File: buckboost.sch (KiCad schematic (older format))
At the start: 24 parts, among them K1 CONN_3, SW1 SPST, U1 TPS63060

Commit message: Added preview for XFL4020 Coilcraft footprint.
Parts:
- C1, C2, C3, C4, C5, C6, C7: footprint (none) -> Capacitors_SMD:C_0805_HandSoldering
- D2, D3: footprint (none) -> LEDs:LED_0805
- K1: footprint (none) -> Pin_Headers:Pin_Header_Straight_1x03
- L1: footprint (none) -> XFL4020:XFL4020
- R1, R2, R3, R4, R5, R6, R7, R8: footprint (none) -> Resistors_SMD:R_0805_HandSoldering
- SW1: footprint (none) -> Buttons_Switches_ThroughHole:SW_DIP_x1_Slide
- U1: footprint (none) -> Housings_DFN_QFN:DFN-10-1EP_3x3mm_Pitch0.5mm
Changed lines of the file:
@@
 LIBS:valves
 LIBS:tps63060
+LIBS:buckboost-cache
 EELAYER 25 0
 EELAYER END
@@
 F 0 "U1" H 4950 5000 60  0000 C CNN
 F 1 "TPS63060" H 4950 4200 60  0000 C CNN
-F 2 "" H 4950 4150 60  0000 C CNN
+F 2 "Housings_DFN_QFN:DFN-10-1EP_3x3mm_Pitch0.5mm" H 4950 4150 60  0001 C CNN
 F 3 "" H 4950 4150 60  0000 C CNN
 	1    4950 4150
@@
 F 0 "C2" H 3550 3800 40  0000 L CNN
 F 1 "0.1 uF" H 3556 3615 40  0000 L CNN
-F 2 "" H 3588 3550 30  0000 C CNN
+F 2 "Capacitors_SMD:C_0805_HandSoldering" H 3588 3550 30  0001 C CNN
 F 3 "" H 3550 3700 60  0000 C CNN
 	1    3550 3700
@@
 F 0 "L1" V 4900 3100 40  0000 C CNN
 F 1 "1 uH" V 5050 3100 40  0000 C CNN
-F 2 "" H 4950 3100 60  0000 C CNN
+F 2 "XFL4020:XFL4020" H 4950 3100 60  0001 C CNN
 F 3 "" H 4950 3100 60  0000 C CNN
 	1    4950 3100
@@
 F 0 "C3" H 4150 4400 40  0000 L CNN
 F 1 "0.1 uF" H 4156 4215 40  0000 L CNN
-F 2 "" H 4188 4150 30  0000 C CNN
+F 2 "Capacitors_SMD:C_0805_HandSoldering" H 4188 4150 30  0001 C CNN
 F 3 "" H 4150 4300 60  0000 C CNN
 	1    4150 4300
@@
 F 0 "R4" V 5930 3600 40  0000 C CNN
 F 1 "1M R" V 5857 3601 40  0000 C CNN
-F 2 "" V 5780 3600 30  0000 C CNN
+F 2 "Resistors_SMD:R_0805_HandSoldering" V 5780 3600 30  0001 C CNN
 F 3 "" H 5850 3600 30  0000 C CNN
 	1    5850 3600
@@
 F 0 "C4" H 6350 4050 40  0000 L CNN
 F 1 "10 pF" H 6356 3865 40  0000 L CNN
-F 2 "" H 6388 3800 30  0000 C CNN
+F 2 "Capacitors_SMD:C_0805_HandSoldering" H 6388 3800 30  0001 C CNN
 F 3 "" H 6350 3950 60  0000 C CNN
 	1    6350 3950
@@
 F 0 "R6" V 7030 3950 40  0000 C CNN
 F 1 "1M R" V 6957 3951 40  0000 C CNN
-F 2 "" V 6880 3950 30  0000 C CNN
+F 2 "Resistors_SMD:R_0805_HandSoldering" V 6880 3950 30  0001 C CNN
 F 3 "" H 6950 3950 30  0000 C CNN
 	1    6950 3950
@@
 F 0 "C5" H 8050 3800 40  0000 L CNN
 F 1 "22uF" H 8056 3615 40  0000 L CNN
-F 2 "" H 8088 3550 30  0000 C CNN
+F 2 "Capacitors_SMD:C_0805_HandSoldering" H 8088 3550 30  0001 C CNN
 F 3 "" H 8050 3700 60  0000 C CNN
 	1    8050 3700
@@
 F 0 "C1" H 3200 3800 40  0000 L CNN
 F 1 "10 uF" H 3206 3615 40  0000 L CNN
-F 2 "" H 3238 3550 30  0000 C CNN
+F 2 "Capacitors_SMD:C_0805_HandSoldering" H 3238 3550 30  0001 C CNN
 F 3 "" H 3200 3700 60  0000 C CNN
 	1    3200 3700
@@
 F 0 "C6" H 8300 3800 40  0000 L CNN
 F 1 "22uF" H 8306 3615 40  0000 L CNN
-F 2 "" H 8338 3550 30  0000 C CNN
+F 2 "Capacitors_SMD:C_0805_HandSoldering" H 8338 3550 30  0001 C CNN
 F 3 "" H 8300 3700 60  0000 C CNN
 	1    8300 3700
@@
 F 0 "C7" H 8550 3800 40  0000 L CNN
 F 1 "22uF" H 8556 3615 40  0000 L CNN
-F 2 "" H 8588 3550 30  0000 C CNN
+F 2 "Capacitors_SMD:C_0805_HandSoldering" H 8588 3550 30  0001 C CNN
 F 3 "" H 8550 3700 60  0000 C CNN
 	1    8550 3700
@@
 F 0 "SW1" H 1200 3600 70  0000 C CNN
 F 1 "SPST" H 1200 3400 70  0000 C CNN
-F 2 "" H 1200 3500 60  0000 C CNN
+F 2 "Buttons_Switches_ThroughHole:SW_DIP_x1_Slide" H 1200 3500 60  0001 C CNN
 F 3 "" H 1200 3500 60  0000 C CNN
 	1    1200 3500
@@
 F 0 "D1" H 700 3100 40  0000 C CNN
 F 1 "DIODESCH" H 700 2900 40  0000 C CNN
-F 2 "" H 700 3000 60  0000 C CNN
+F 2 "" H 700 3000 60  0001 C CNN
 F 3 "" H 700 3000 60  0000 C CNN
 	1    700  3000
@@
 F 0 "R5" V 6530 3100 40  0000 C CNN
 F 1 "22k R" V 6457 3101 40  0000 C CNN
-F 2 "" V 6380 3100 30  0000 C CNN
+F 2 "Resistors_SMD:R_0805_HandSoldering" V 6380 3100 30  0001 C CNN
 F 3 "" H 6450 3100 30  0000 C CNN
 	1    6450 3100
@@
 F 0 "D3" H 6850 2950 50  0000 C CNN
 F 1 "LED" H 6850 2750 50  0000 C CNN
-F 2 "" H 6850 2850 60  0000 C CNN
+F 2 "LEDs:LED_0805" H 6850 2850 60  0001 C CNN
 F 3 "" H 6850 2850 60  0000 C CNN
 	1    6850 2850
@@
 F 0 "R3" V 3030 3750 40  0000 C CNN
 F 1 "22k R" V 2957 3751 40  0000 C CNN
-F 2 "" V 2880 3750 30  0000 C CNN
+F 2 "Resistors_SMD:R_0805_HandSoldering" V 2880 3750 30  0001 C CNN
 F 3 "" H 2950 3750 30  0000 C CNN
 	1    2950 3750
@@
 F 0 "D2" H 2950 4400 50  0000 C CNN
 F 1 "LED" H 2950 4200 50  0000 C CNN
-F 2 "" H 2950 4300 60  0000 C CNN
+F 2 "LEDs:LED_0805" H 2950 4300 60  0001 C CNN
 F 3 "" H 2950 4300 60  0000 C CNN
 	1    2950 4300
@@
 F 0 "K1" V 1800 1000 50  0000 C CNN
 F 1 "CONN_3" V 1900 1000 40  0000 C CNN
-F 2 "" H 1850 1000 60  0000 C CNN
+F 2 "Pin_Headers:Pin_Header_Straight_1x03" H 1850 1000 60  0001 C CNN
 F 3 "" H 1850 1000 60  0000 C CNN
 	1    1850 1000
@@
 F 0 "R2" V 1580 1450 40  0000 C CNN
 F 1 "111k R" V 1507 1451 40  0000 C CNN
-F 2 "" V 1430 1450 30  0000 C CNN
+F 2 "Resistors_SMD:R_0805_HandSoldering" V 1430 1450 30  0001 C CNN
 F 3 "" H 1500 1450 30  0000 C CNN
 	1    1500 1450
@@
 F 0 "R1" V 830 1450 40  0000 C CNN
 F 1 "179k R" V 757 1451 40  0000 C CNN
-F 2 "" V 680 1450 30  0000 C CNN
+F 2 "Resistors_SMD:R_0805_HandSoldering" V 680 1450 30  0001 C CNN
 F 3 "" H 750 1450 30  0000 C CNN
 	1    750  1450
@@
 F 0 "FB1" H 2150 3600 50  0000 C CNN
 F 1 "1K @ 100 MHz" H 2150 3450 50  0000 C CNN
-F 2 "" H 2150 3500 60  0000 C CNN
+F 2 "" H 2150 3500 60  0001 C CNN
 F 3 "" H 2150 3500 60  0000 C CNN
 	1    2150 3500
@@
 F 0 "FB2" H 7600 3600 50  0000 C CNN
 F 1 "1K @ 100 MHz" H 7600 3450 50  0000 C CNN
-F 2 "" H 7600 3500 60  0000 C CNN
+F 2 "" H 7600 3500 60  0001 C CNN
 F 3 "" H 7600 3500 60  0000 C CNN
 	1    7600 3500
@@
 F 0 "R8" V 8980 3500 40  0000 C CNN
 F 1 "0.01" V 8907 3501 40  0000 C CNN
-F 2 "" V 8830 3500 30  0000 C CNN
+F 2 "Resistors_SMD:R_0805_HandSoldering" V 8830 3500 30  0001 C CNN
 F 3 "" H 8900 3500 30  0000 C CNN
 	1    8900 3500
@@
 F 0 "R7" V 4180 3500 40  0000 C CNN
 F 1 "0.01" V 4107 3501 40  0000 C CNN
-F 2 "" V 4030 3500 30  0000 C CNN
+F 2 "Resistors_SMD:R_0805_HandSoldering" V 4030 3500 30  0001 C CNN
 F 3 "" H 4100 3500 30  0000 C CNN
 	1    4100 3500

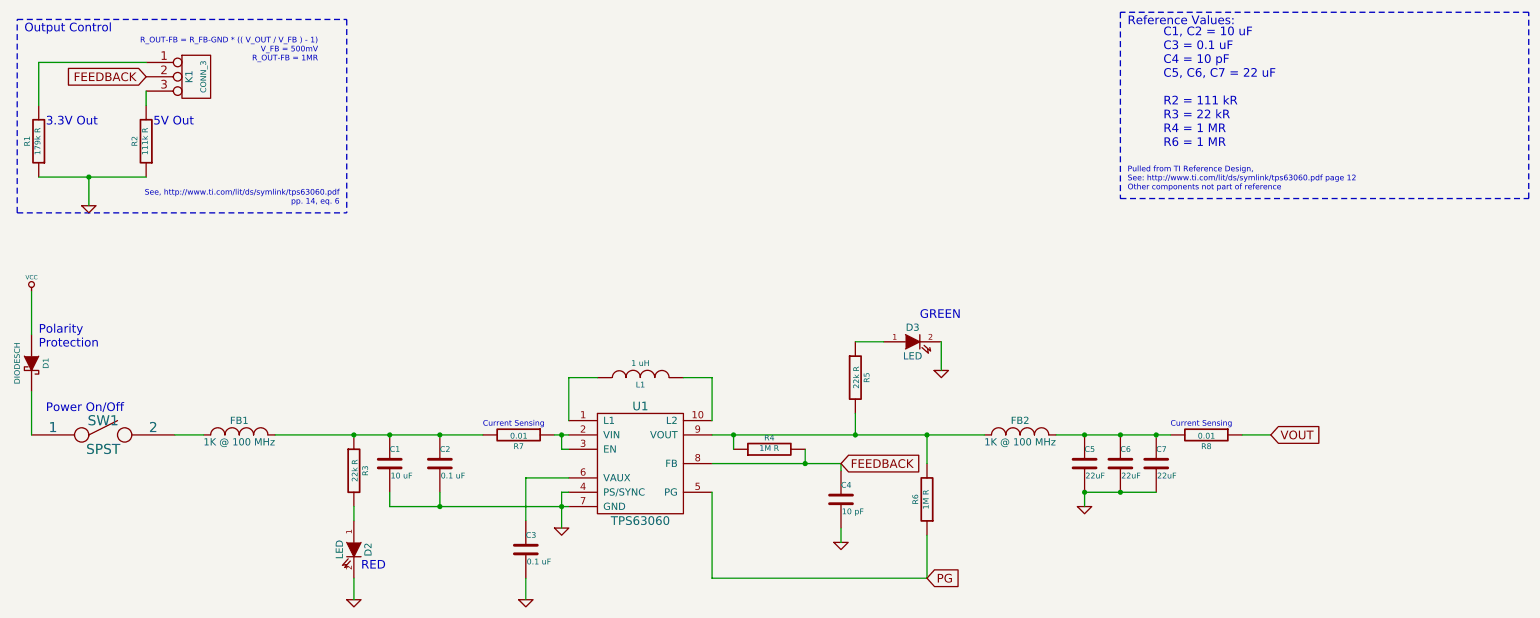
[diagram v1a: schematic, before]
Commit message: Footprints chosen, PCB starting. No preview.
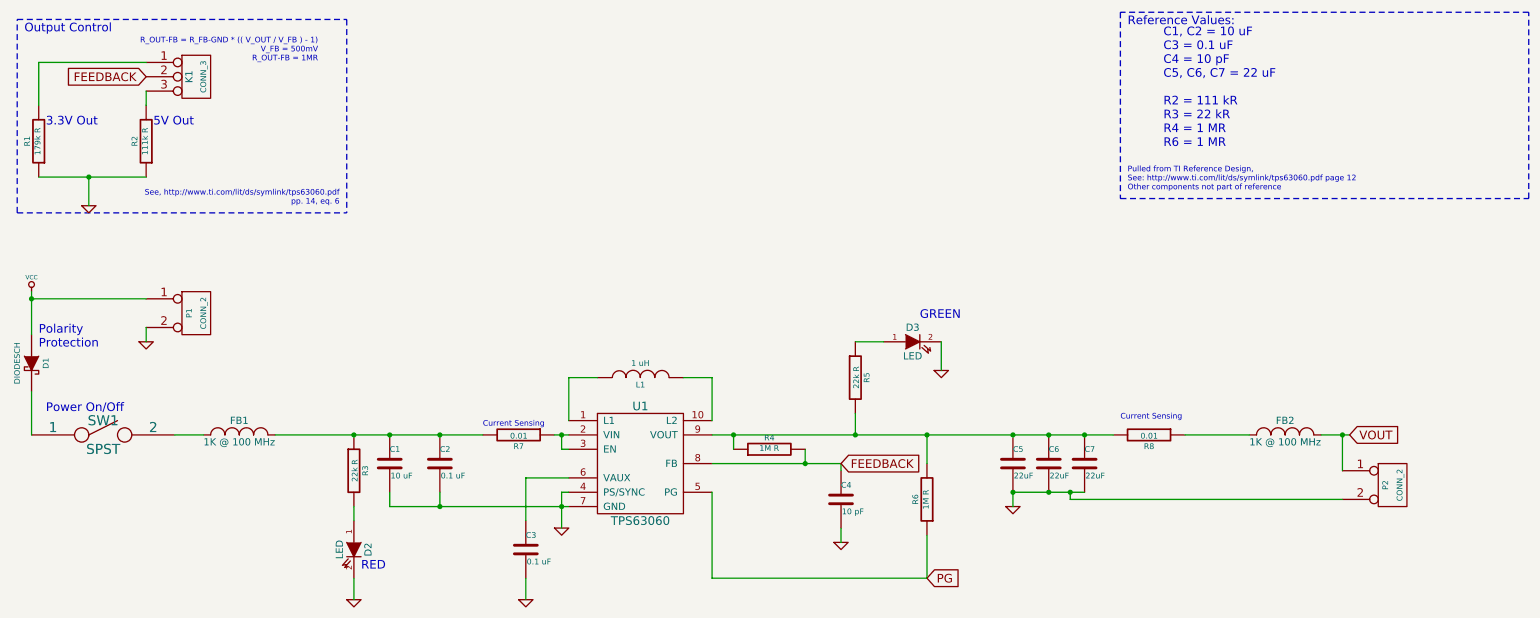
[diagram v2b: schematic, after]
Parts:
- added P1, P2: CONN_2, Pin_Headers:Pin_Header_Straight_1x02, symbol CONN_2
- D1: footprint (none) -> Capacitors_SMD:C_1206_HandSoldering
- FB1, FB2: footprint (none) -> Capacitors_SMD:C_1210_HandSoldering
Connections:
- net GND: now also P1.2 (PM), P2.2 (PM)
- net VCC: now also P1.1 (P1)
- net VOUT: now also FB2.2, P2.1 (P1); no longer R8.1
- net at R4.1, R5.2, R6.2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: now also C5.1, C6.1, C7.1, R8.2; no longer FB2.1
- new net: FB2.1, R8.1
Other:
- moved on the sheet: C5, C6, C7, FB2, R8
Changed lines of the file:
@@
 L C C5
 U 1 1 56ED0F3F
-P 8050 3700
-F 0 "C5" H 8050 3800 40  0000 L CNN
-F 1 "22uF" H 8056 3615 40  0000 L CNN
-F 2 "Capacitors_SMD:C_0805_HandSoldering" H 8088 3550 30  0001 C CNN
-F 3 "" H 8050 3700 60  0000 C CNN
-	1    8050 3700
+P 7550 3700
+F 0 "C5" H 7550 3800 40  0000 L CNN
+F 1 "22uF" H 7556 3615 40  0000 L CNN
+F 2 "Capacitors_SMD:C_0805_HandSoldering" H 7588 3550 30  0001 C CNN
+F 3 "" H 7550 3700 60  0000 C CNN
+	1    7550 3700
 	1    0    0    -1
 $EndComp
@@
 L GND #PWR05
 U 1 1 56ED0F95
-P 8050 4000
-F 0 "#PWR05" H 8050 4000 30  0001 C CNN
-F 1 "GND" H 8050 3930 30  0001 C CNN
-F 2 "" H 8050 4000 60  0000 C CNN
-F 3 "" H 8050 4000 60  0000 C CNN
-	1    8050 4000
-	1    0    0    -1
-$EndComp
-Text GLabel 9350 3500 2    60   Input ~ 0
+P 7550 4000
+F 0 "#PWR05" H 7550 4000 30  0001 C CNN
+F 1 "GND" H 7550 3930 30  0001 C CNN
+F 2 "" H 7550 4000 60  0000 C CNN
+F 3 "" H 7550 4000 60  0000 C CNN
+	1    7550 4000
+	1    0    0    -1
+$EndComp
+Text GLabel 9900 3500 2    60   Input ~ 0
 VOUT
 Text GLabel 6950 4500 2    60   Input ~ 0
@@
 L C C6
 U 1 1 56ED199B
-P 8300 3700
-F 0 "C6" H 8300 3800 40  0000 L CNN
-F 1 "22uF" H 8306 3615 40  0000 L CNN
-F 2 "Capacitors_SMD:C_0805_HandSoldering" H 8338 3550 30  0001 C CNN
-F 3 "" H 8300 3700 60  0000 C CNN
-	1    8300 3700
+P 7800 3700
+F 0 "C6" H 7800 3800 40  0000 L CNN
+F 1 "22uF" H 7806 3615 40  0000 L CNN
+F 2 "Capacitors_SMD:C_0805_HandSoldering" H 7838 3550 30  0001 C CNN
+F 3 "" H 7800 3700 60  0000 C CNN
+	1    7800 3700
 	1    0    0    -1
 $EndComp
@@
 L C C7
 U 1 1 56ED19D2
-P 8550 3700
-F 0 "C7" H 8550 3800 40  0000 L CNN
-F 1 "22uF" H 8556 3615 40  0000 L CNN
-F 2 "Capacitors_SMD:C_0805_HandSoldering" H 8588 3550 30  0001 C CNN
-F 3 "" H 8550 3700 60  0000 C CNN
-	1    8550 3700
+P 8050 3700
+F 0 "C7" H 8050 3800 40  0000 L CNN
+F 1 "22uF" H 8056 3615 40  0000 L CNN
+F 2 "Capacitors_SMD:C_0805_HandSoldering" H 8088 3550 30  0001 C CNN
+F 3 "" H 8050 3700 60  0000 C CNN
+	1    8050 3700
 	1    0    0    -1
 $EndComp
@@
 F 0 "D1" H 700 3100 40  0000 C CNN
 F 1 "DIODESCH" H 700 2900 40  0000 C CNN
-F 2 "" H 700 3000 60  0001 C CNN
+F 2 "Capacitors_SMD:C_1206_HandSoldering" H 700 3000 60  0001 C CNN
 F 3 "" H 700 3000 60  0000 C CNN
 	1    700  3000
@@
 Text GLabel 6350 3700 2    60   Input ~ 0
 FEEDBACK
-Wire Wire Line
-	5450 3400 5450 3100
-Wire Wire Line
-	5450 3100 5250 3100
-Wire Wire Line
-	4450 3400 4450 3100
-Wire Wire Line
-	4450 3100 4650 3100
-Wire Wire Line
-	4400 3900 4400 4150
-Connection ~ 4400 4000
-Wire Wire Line
-	4450 3800 4150 3800
-Wire Wire Line
-	4150 3800 4150 4100
-Wire Wire Line
-	4150 4500 4150 4650
-Wire Wire Line
-	4450 3900 4400 3900
-Wire Wire Line
-	5450 3700 6350 3700
-Wire Wire Line
-	5450 3500 7350 3500
-Wire Wire Line
-	5600 3500 5600 3600
-Wire Wire Line
-	6100 3700 6100 3600
-Connection ~ 6100 3700
-Wire Wire Line
-	6350 3700 6350 3750
-Wire Wire Line
-	6350 4150 6350 4250
-Connection ~ 5600 3500
-Wire Wire Line
-	6950 3500 6950 3700
-Wire Wire Line
-	5450 3900 5450 4500
-Wire Wire Line
-	5450 4500 6950 4500
-Wire Wire Line
-	6950 4500 6950 4200
-Wire Wire Line
-	8050 3900 8050 4000
-Connection ~ 6950 3500
-Wire Wire Line
-	3200 4000 4450 4000
-Wire Wire Line
-	8050 3900 8550 3900
-Connection ~ 8300 3900
-Connection ~ 8050 3900
-Wire Wire Line
-	700  2500 700  2800
-Wire Wire Line
-	700  3200 700  3500
-Wire Wire Line
-	7050 2850 7050 3050
-Wire Wire Line
-	6450 2850 6650 2850
-Wire Wire Line
-	6450 3350 6450 3500
-Connection ~ 6450 3500
-Connection ~ 2950 3500
-Wire Wire Line
-	2950 4000 2950 4100
-Wire Wire Line
-	2950 4500 2950 4650
-Wire Notes Line
-	11150 550  8300 550
 Text GLabel 1500 1000 0    60   Input ~ 0
 FEEDBACK
@@
 	-1   0    0    1
 $EndComp
-Wire Wire Line
-	1500 1100 1500 1200
-Wire Wire Line
-	1500 900  750  900
-Wire Wire Line
-	750  900  750  1200
 $Comp
 L GND #PWR08
@@
 	1    0    0    -1
 $EndComp
-Wire Wire Line
-	750  1700 1500 1700
-Wire Wire Line
-	1100 1700 1100 1900
-Connection ~ 1100 1700
 Text Notes 1550 1350 0    60   ~ 0
 5V Out
@@
 Text Notes 8600 1500 0    60   ~ 0
 C1, C2 = 10 uF\nC3 = 0.1 uF\nC4 = 10 pF\nC5, C6, C7 = 22 uF\n\nR2 = 111 kR\nR3 = 22 kR\nR4 = 1 MR\nR6 = 1 MR\n
-Wire Notes Line
-	8300 1850 11150 1850
-Wire Notes Line
-	8300 550  8300 1850
-Wire Notes Line
-	11150 1850 11150 550
-Wire Notes Line
-	600  1950 2900 1950
-Wire Notes Line
-	600  1950 600  600
-Wire Notes Line
-	600  600  2900 600
-Wire Notes Line
-	2900 600  2900 1950
 $Comp
 L INDUCTOR_SMALL FB1
@@
 F 0 "FB1" H 2150 3600 50  0000 C CNN
 F 1 "1K @ 100 MHz" H 2150 3450 50  0000 C CNN
-F 2 "" H 2150 3500 60  0001 C CNN
+F 2 "Capacitors_SMD:C_1210_HandSoldering" H 2150 3500 60  0001 C CNN
 F 3 "" H 2150 3500 60  0000 C CNN
 	1    2150 3500
 	1    0    0    -1
 $EndComp
-Wire Wire Line
-	7850 3500 8650 3500
-Wire Wire Line
-	1700 3500 1900 3500
 $Comp
 L INDUCTOR_SMALL FB2
 U 1 1 56F01A9C
-P 7600 3500
-F 0 "FB2" H 7600 3600 50  0000 C CNN
-F 1 "1K @ 100 MHz" H 7600 3450 50  0000 C CNN
-F 2 "" H 7600 3500 60  0001 C CNN
-F 3 "" H 7600 3500 60  0000 C CNN
-	1    7600 3500
+P 9450 3500
+F 0 "FB2" H 9450 3600 50  0000 C CNN
+F 1 "1K @ 100 MHz" H 9450 3450 50  0000 C CNN
+F 2 "Capacitors_SMD:C_1210_HandSoldering" H 9450 3500 60  0001 C CNN
+F 3 "" H 9450 3500 60  0000 C CNN
+	1    9450 3500
 	1    0    0    -1
 $EndComp
@@
 L R R8
 U 1 1 56F01F50
-P 8900 3500
-F 0 "R8" V 8980 3500 40  0000 C CNN
-F 1 "0.01" V 8907 3501 40  0000 C CNN
-F 2 "Resistors_SMD:R_0805_HandSoldering" V 8830 3500 30  0001 C CNN
-F 3 "" H 8900 3500 30  0000 C CNN
-	1    8900 3500
+P 8500 3500
+F 0 "R8" V 8580 3500 40  0000 C CNN
+F 1 "0.01" V 8507 3501 40  0000 C CNN
+F 2 "Resistors_SMD:R_0805_HandSoldering" V 8430 3500 30  0001 C CNN
+F 3 "" H 8500 3500 30  0000 C CNN
+	1    8500 3500
 	0    1    1    0
 $EndComp
-Connection ~ 8050 3500
-Connection ~ 8300 3500
-Connection ~ 8550 3500
-Wire Wire Line
-	9150 3500 9350 3500
 $Comp
 L R R7
@@
 	0    1    1    0
 $EndComp
+Text Notes 3850 3450 0    39   ~ 0
+Current Sensing
+Text Notes 8300 3400 0    39   ~ 0
+Current Sensing
+$Comp
+L CONN_2 P1
+U 1 1 5705A13F
+P 1850 2650
+F 0 "P1" V 1800 2650 40  0000 C CNN
+F 1 "CONN_2" V 1900 2650 40  0000 C CNN
+F 2 "Pin_Headers:Pin_Header_Straight_1x02" H 1850 2650 60  0001 C CNN
+F 3 "" H 1850 2650 60  0000 C CNN
+	1    1850 2650
+	1    0    0    -1
+$EndComp
+Wire Wire Line
+	5450 3400 5450 3100
+Wire Wire Line
+	5450 3100 5250 3100
+Wire Wire Line
+	4450 3400 4450 3100
+Wire Wire Line
+	4450 3100 4650 3100
+Wire Wire Line
+	4400 3900 4400 4150
+Connection ~ 4400 4000
+Wire Wire Line
+	4450 3800 4150 3800
+Wire Wire Line
+	4150 3800 4150 4100
+Wire Wire Line
+	4150 4500 4150 4650
+Wire Wire Line
+	4450 3900 4400 3900
+Wire Wire Line
+	5450 3700 6350 3700
+Wire Wire Line
+	5450 3500 8250 3500
+Wire Wire Line
+	5600 3500 5600 3600
+Wire Wire Line
+	6100 3700 6100 3600
+Connection ~ 6100 3700
+Wire Wire Line
+	6350 3700 6350 3750
+Wire Wire Line
+	6350 4150 6350 4250
+Connection ~ 5600 3500
+Wire Wire Line
+	6950 3500 6950 3700
+Wire Wire Line
+	5450 3900 5450 4500
+Wire Wire Line
+	5450 4500 6950 4500
+Wire Wire Line
+	6950 4500 6950 4200
+Wire Wire Line
+	7550 3900 7550 4000
+Connection ~ 6950 3500
+Wire Wire Line
+	3200 4000 4450 4000
+Wire Wire Line
+	7550 3900 8050 3900
+Connection ~ 7800 3900
+Connection ~ 7550 3900
+Wire Wire Line
+	700  2500 700  2800
+Wire Wire Line
+	700  3200 700  3500
+Wire Wire Line
+	7050 2850 7050 3050
+Wire Wire Line
+	6450 2850 6650 2850
+Wire Wire Line
+	6450 3350 6450 3500
+Connection ~ 6450 3500
+Connection ~ 2950 3500
+Wire Wire Line
+	2950 4000 2950 4100
+Wire Wire Line
+	2950 4500 2950 4650
+Wire Notes Line
+	11150 550  8300 550
+Wire Wire Line
+	1500 1100 1500 1200
+Wire Wire Line
+	1500 900  750  900
+Wire Wire Line
+	750  900  750  1200
+Wire Wire Line
+	750  1700 1500 1700
+Wire Wire Line
+	1100 1700 1100 1900
+Connection ~ 1100 1700
+Wire Notes Line
+	8300 1850 11150 1850
+Wire Notes Line
+	8300 550  8300 1850
+Wire Notes Line
+	11150 1850 11150 550
+Wire Notes Line
+	600  1950 2900 1950
+Wire Notes Line
+	600  1950 600  600
+Wire Notes Line
+	600  600  2900 600
+Wire Notes Line
+	2900 600  2900 1950
+Wire Wire Line
+	1700 3500 1900 3500
+Connection ~ 7550 3500
+Connection ~ 7800 3500
+Connection ~ 8050 3500
+Wire Wire Line
+	9700 3500 9900 3500
 Wire Wire Line
 	3200 4000 3200 3900
@@
 Wire Wire Line
 	3850 3500 2400 3500
-Text Notes 3850 3450 0    39   ~ 0
-Current Sensing
-Text Notes 8650 3450 0    39   ~ 0
-Current Sensing
+Wire Wire Line
+	9200 3500 8750 3500
+Wire Wire Line
+	1500 2550 700  2550
+Connection ~ 700  2550
+$Comp
+L GND #PWR09
+U 1 1 5705AF2B
+P 1500 2850
+F 0 "#PWR09" H 1500 2850 30  0001 C CNN
+F 1 "GND" H 1500 2780 30  0001 C CNN
+F 2 "" H 1500 2850 60  0000 C CNN
+F 3 "" H 1500 2850 60  0000 C CNN
+	1    1500 2850
+	1    0    0    -1
+$EndComp
+Wire Wire Line
+	1500 2750 1500 2850
+$Comp
+L CONN_2 P2
+U 1 1 5705B0DB
+P 10200 3850
+F 0 "P2" V 10150 3850 40  0000 C CNN
+F 1 "CONN_2" V 10250 3850 40  0000 C CNN
+F 2 "Pin_Headers:Pin_Header_Straight_1x02" H 10200 3850 60  0001 C CNN
+F 3 "" H 10200 3850 60  0000 C CNN
+	1    10200 3850
+	1    0    0    -1
+$EndComp
+Wire Wire Line
+	9850 3750 9850 3500
+Connection ~ 9850 3500
+Wire Wire Line
+	9850 3950 7950 3950
+Wire Wire Line
+	7950 3950 7950 3900
+Connection ~ 7950 3900
 $EndSCHEMATC
